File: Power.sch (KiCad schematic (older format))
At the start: 27 parts, among them J3 Conn_01x02, Q1 MMBT5401LT1G, Q2 Q_NMOS_GDS, Q3 MMBT3904, Q4 Q_NMOS_GDS, U6 LM5066

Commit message: Added protection from motor regeneration through capacitors + MOSFET, started placement and routing
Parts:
- added C32, C33, C34, C35, C36, C37: 330u, Capacitor_SMD:CP_Elec_18x17.5, symbol Device:CP_Small
- added C38, C39: 1u, Capacitor_SMD:C_0603_1608Metric, symbol Device:C_Small
- added C40: 100n, Capacitor_SMD:C_0603_1608Metric, symbol Device:C_Small
- added J4: Conn_01x02, Connector_PinHeader_2.54mm:PinHeader_1x02_P2.54mm_Horizontal, symbol Connector_Generic:Conn_01x02
- added Q5: Q_NMOS_GDS, Package_TO_SOT_SMD:TO-263-2, symbol Device:Q_NMOS_GDS
- added R21: 10R, Package_TO_SOT_THT:TO-247-2_Vertical, symbol Device:R_Small
- added R22: 100k, Resistor_SMD:R_0603_1608Metric, symbol Device:R_Small
- added R23: 49.9k, Resistor_SMD:R_0603_1608Metric, symbol Device:R_Small
- added R24: 2.7k, Resistor_SMD:R_0603_1608Metric, symbol Device:R_Small
- added R25: 82.5k, Resistor_SMD:R_0805_2012Metric, symbol Device:R_Small
- added R26, R28: 24.9k, Resistor_SMD:R_0805_2012Metric, symbol Device:R_Small
- added R27: 75k, Resistor_SMD:R_0805_2012Metric, symbol Device:R_Small
- added R29: 2M, Resistor_SMD:R_0603_1608Metric, symbol Device:R_Small
- added U7: LM311, Package_SO:SOIC-8_3.9x4.9mm_P1.27mm, symbol Comparator:LM311
- added U8: LR8K4-G, Package_TO_SOT_SMD:TO-252-2, symbol Regulator_Linear:LR8K4-G
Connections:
- net labels added: +24V, PROT_DRAIN
- wire segments 102 -> 155
- no-connect marks 5 -> 7
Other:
- note added: "Assuming VIN = 48V, Schmitt trigger\nTurn on at 52.1\nTurn off at 51.1"
- note added: "TODO power resistor and capacitance"
- note added: "TODO: Check if pin header compatible with Anderson connector"
- note added: "TODO: Check input cap for LDO"
- moved on the sheet: D5, D6, Q4, R18, R19, R20

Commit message: WIP with component placement
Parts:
- removed C33, C34, C35, C36, C37: 330u, Capacitor_SMD:CP_Elec_18x17.5, symbol Device:CP_Small
- removed C40: 100n, Capacitor_SMD:C_0603_1608Metric, symbol Device:C_Small
- removed R29: 2M, Resistor_SMD:R_0603_1608Metric, symbol Device:R_Small
- removed U7: LM311, Package_SO:SOIC-8_3.9x4.9mm_P1.27mm, symbol Comparator:LM311
- added C33, C34, C35: 100n, Capacitor_SMD:C_0603_1608Metric, symbol Device:C_Small
- added C36: 1nF, Capacitor_SMD:C_0603_1608Metric, symbol Device:C_Small
- added J5: Conn_ARM_JTAG_SWD_10, Connector_PinHeader_1.27mm:PinHeader_2x05_P1.27mm_Vertical, symbol Connector:Conn_ARM_JTAG_SWD_10
- added U7: STM32L011K4Tx, Package_QFP:LQFP-32_7x7mm_P0.8mm, symbol MCU_ST_STM32L0:STM32L011K4Tx
- C32: value 330u -> 470u
- C38: footprint Capacitor_SMD:C_0603_1608Metric -> Capacitor_SMD:C_1206_3216Metric
- C39: footprint Capacitor_SMD:C_0603_1608Metric -> Capacitor_SMD:C_0805_2012Metric
- J4: footprint Connector_PinHeader_2.54mm:PinHeader_1x02_P2.54mm_Horizontal -> Connectors_OSRF:PP45_1X2
- R23: value 49.9k -> 18.2K
- R24: value 2.7k -> 11.5K
- R25: value 82.5k -> 82.9k
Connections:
- net labels added: +3.3VP, SWDCLK, SWDIO, nRST
- net labels removed: +24V, PROT_DRAIN
- wire segments 155 -> 162
- no-connect marks 7 -> 5
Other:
- note removed: "Assuming VIN = 48V, Schmitt trigger\nTurn on at 52.1\nTurn off at 51.1"
- moved on the sheet: C29, C32, J3, J4, Q3, Q5, R21, R22, R25, R26, R27, R28

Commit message: Finished schematic, placement and routing, only silkscreen TODO
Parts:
- removed R23: 18.2K, Resistor_SMD:R_0603_1608Metric, symbol Device:R_Small
- removed R24: 11.5K, Resistor_SMD:R_0603_1608Metric, symbol Device:R_Small
- removed U8: LR8K4-G, Package_TO_SOT_SMD:TO-252-2, symbol Regulator_Linear:LR8K4-G
- added C37: 1u, Capacitor_SMD:C_1206_3216Metric, symbol Device:C_Small
- added U9: MAXM15062, DCDC:MAXIM_uSLIP-10, symbol DCDC_Converters:MAXM15062
- C31: footprint Capacitor_SMD:C_0603_1608Metric -> Capacitor_SMD:C_0402_1005Metric
- C38: footprint Capacitor_SMD:C_1206_3216Metric -> Capacitor_SMD:C_0603_1608Metric
- C39: value 1u -> 10u; footprint Capacitor_SMD:C_0805_2012Metric -> Capacitor_SMD:C_1206_3216Metric
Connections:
- net labels removed: LM_VDD
- wire segments 162 -> 168
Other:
- note removed: "TODO power resistor and capacitance"
- note removed: "TODO: Check if pin header compatible with Anderson connector"
- note removed: "TODO: Check input cap for LDO"
- moved on the sheet: C32, C33, C34, C35, J5, Q5, R21, R22, R25, R26, R27, R28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

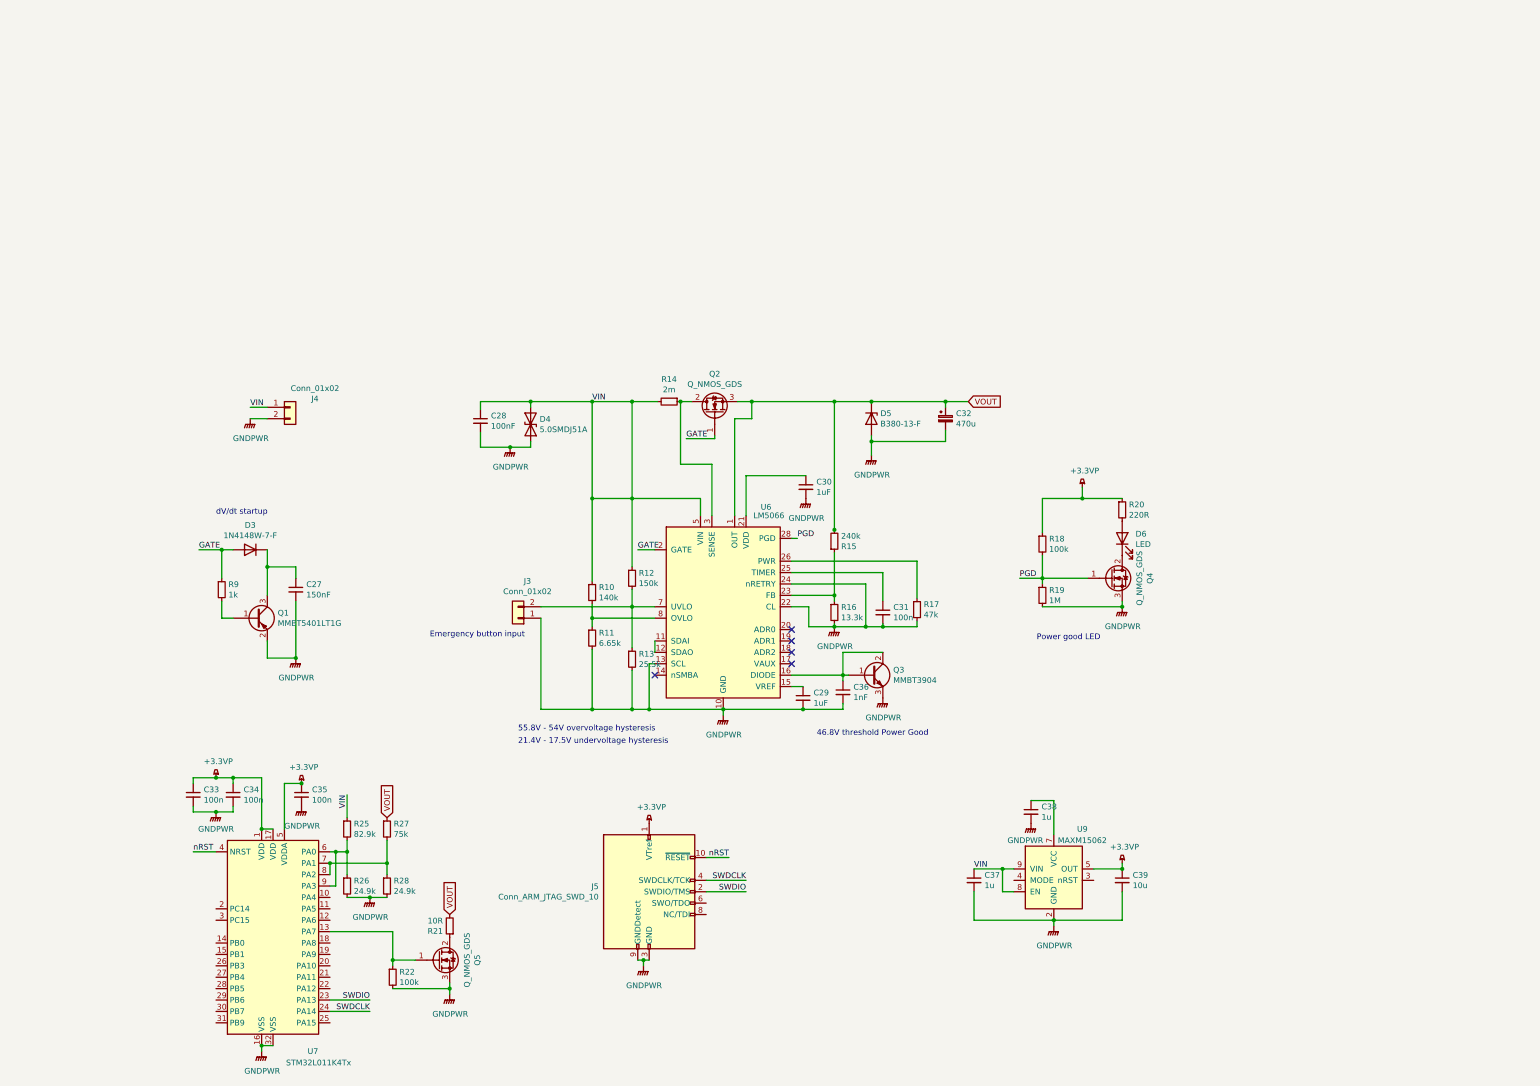
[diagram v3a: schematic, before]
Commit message: Fixed flipped connector, changed most placement
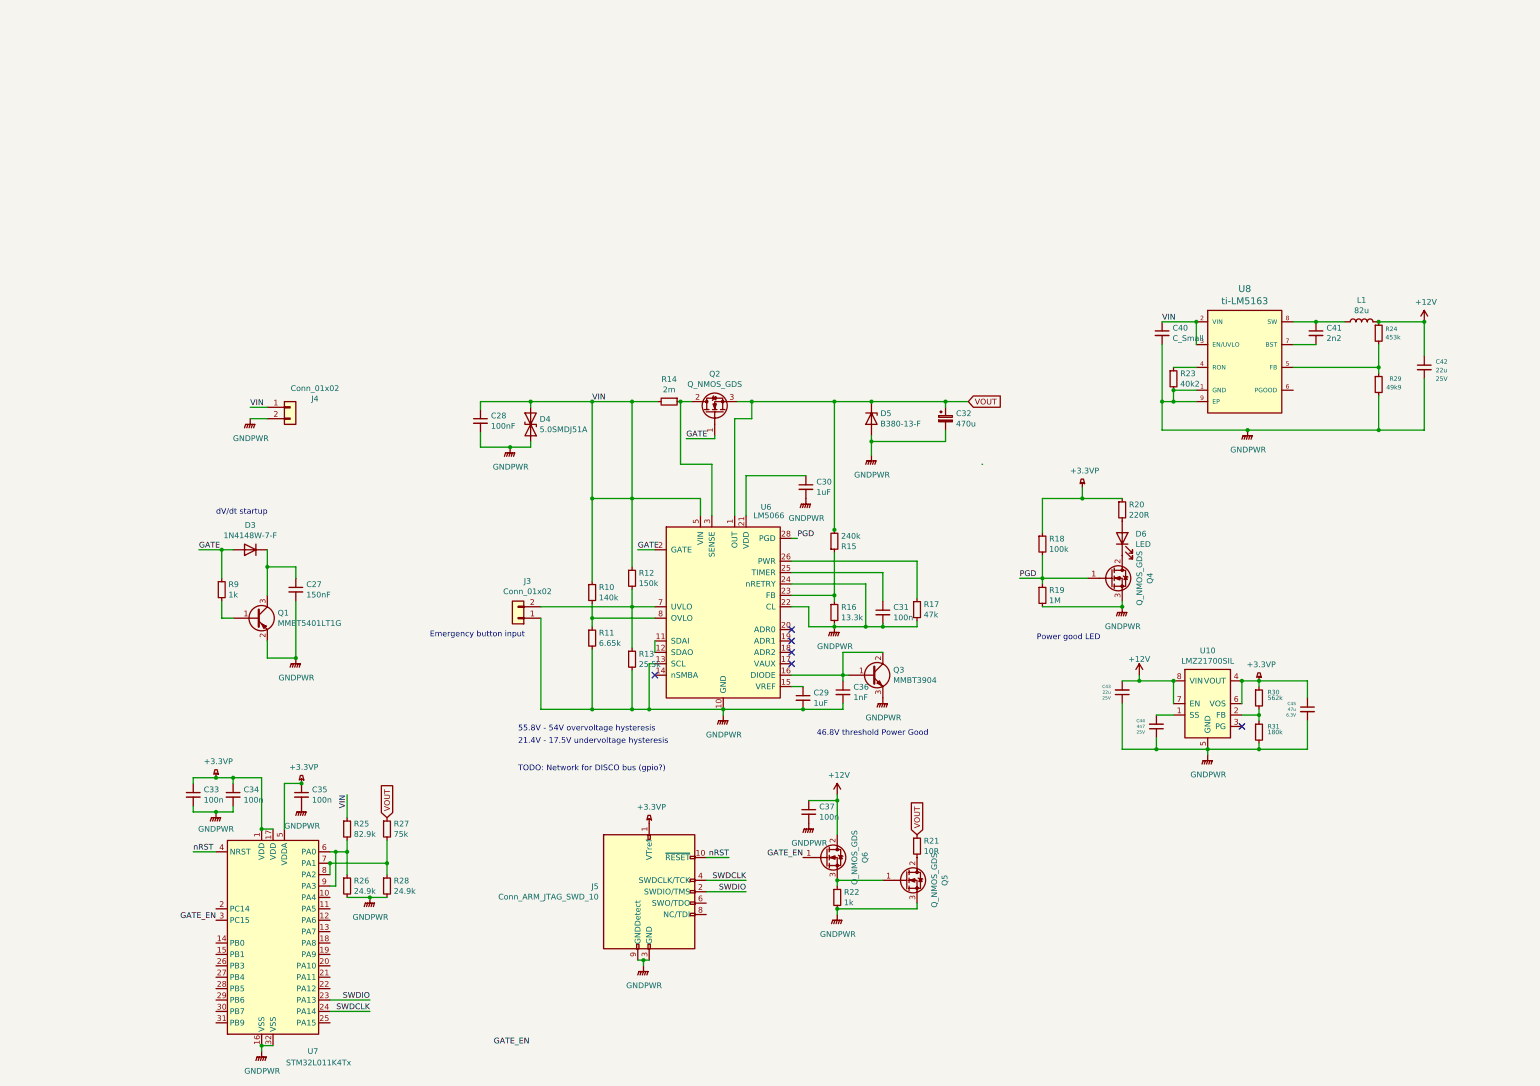
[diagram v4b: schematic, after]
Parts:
- removed C38: 1u, Capacitor_SMD:C_0603_1608Metric, symbol Device:C_Small
- removed C39: 10u, Capacitor_SMD:C_1206_3216Metric, symbol Device:C_Small
- removed U9: MAXM15062, DCDC:MAXIM_uSLIP-10, symbol DCDC_Converters:MAXM15062
- added C40: C_Small, Capacitor_SMD:C_1210_3225Metric, symbol Device:C_Small
- added C41: 2n2, Capacitor_SMD:C_0603_1608Metric, symbol Device:C_Small
- added C42: 22u, Capacitor_SMD:C_1210_3225Metric, symbol Device:C_Small
- added C43: 22u, Capacitor_SMD:C_1206_3216Metric, symbol Device:C_Small
- added C44: 4n7, Capacitor_SMD:C_0402_1005Metric, symbol Device:C_Small
- added C45: 47u, Capacitor_SMD:C_1206_3216Metric, symbol Device:C_Small
- added L1: 82u, Inductor_SMD:L_7.3x7.3_H4.5, symbol Device:L
- added Q6: Q_NMOS_GDS, Package_TO_SOT_SMD:SOT-416, symbol Device:Q_NMOS_GDS
- added R23: 40k2, Resistor_SMD:R_0805_2012Metric, symbol Device:R_Small
- added R24: 453k, Resistor_SMD:R_0603_1608Metric, symbol Device:R_Small
- added R29: 49k9, Resistor_SMD:R_0603_1608Metric, symbol Device:R_Small
- added R30: 562k, Resistor_SMD:R_0402_1005Metric, symbol Device:R_Small
- added R31: 180k, Resistor_SMD:R_0402_1005Metric, symbol Device:R_Small
- added U10: LMZ21700SIL, BLDC:SIL0008E, symbol BLDC:LMZ21700SILT
- added U8: ti-LM5163, Package_SO:SOIC-8-1EP_3.9x4.9mm_P1.27mm_EP2.41x3.3mm, symbol BLDC:ti-LM5163
- C31: footprint Capacitor_SMD:C_0402_1005Metric -> Capacitor_SMD:C_0603_1608Metric
- C37: value 1u -> 100n; footprint Capacitor_SMD:C_1206_3216Metric -> Capacitor_SMD:C_0603_1608Metric
- R22: value 100k -> 1k
- R25, R26, R27, R28: footprint Resistor_SMD:R_0805_2012Metric -> Resistor_SMD:R_0603_1608Metric
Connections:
- net +3.3VP: now also C45.1, R30.1, U10.4 (VOUT), U10.6 (VOS)
- net GNDPWR: now also C40.2, C42.2, C43.1, C44.1, C45.2, R23.2, R29.2, R31.2, U10.5 (GND), U10.9 (PAD), U8.1 (GND), U8.9 (EP)
- net VIN: now also C40.1, U8.2 (VIN), U8.3 (EN/UVLO); no longer C37.1
- net VOUT: now also R21.1; no longer R21.2
- net at Q5.1 (G), R22.1: now also Q6.3 (S); no longer U7.13 (PA7)
- net at Q5.2 (D): now also R21.2; no longer R21.1
- net GATE_EN: now reaches U7.3 (PC15)
- net GATE_EN: now also Q6.1 (G)
- new net: R23.1, U8.4 (RON)
- new net: R24.2, R29.1, U8.5 (FB)
- new net: C41.2, U8.7 (BST)
- new net: C41.1, L1.1, U8.8 (SW)
- new net: C44.2, U10.1 (SS)
- new net: R30.2, R31.1, U10.2 (FB)
- new net +12V: C37.1, C42.1, C43.2, L1.2, Q6.2 (D), R24.1, U10.7 (EN), U10.8 (VIN)
- no-connect marks 5 -> 6
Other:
- note added: "TODO: Network for DISCO bus (gpio?)"
- moved on the sheet: Q5, R21, R22

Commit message: Silk screen and cosmetic fixes
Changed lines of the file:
@@
 Wire Wire Line
 	10695 4600 10700 4600
-Wire Wire Line
-	8270 2100 8275 2100
 Connection ~ 9950 4000
 Connection ~ 10250 4600

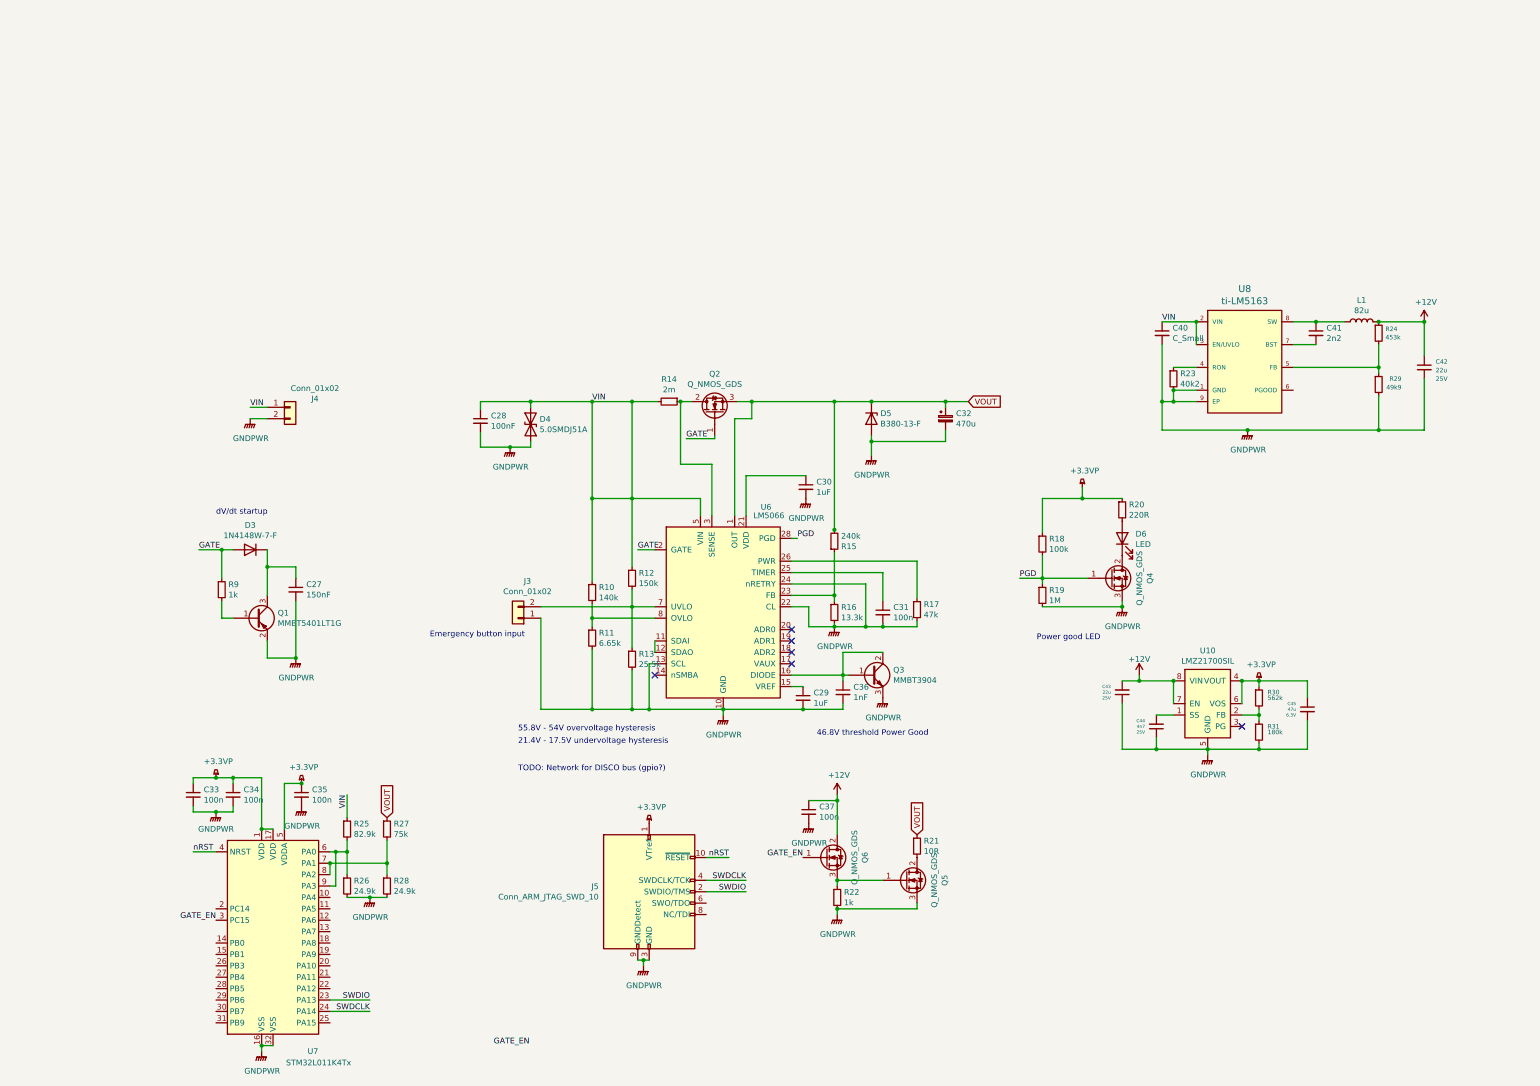
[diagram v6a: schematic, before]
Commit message: Changed voltage regulator, added I2C interface
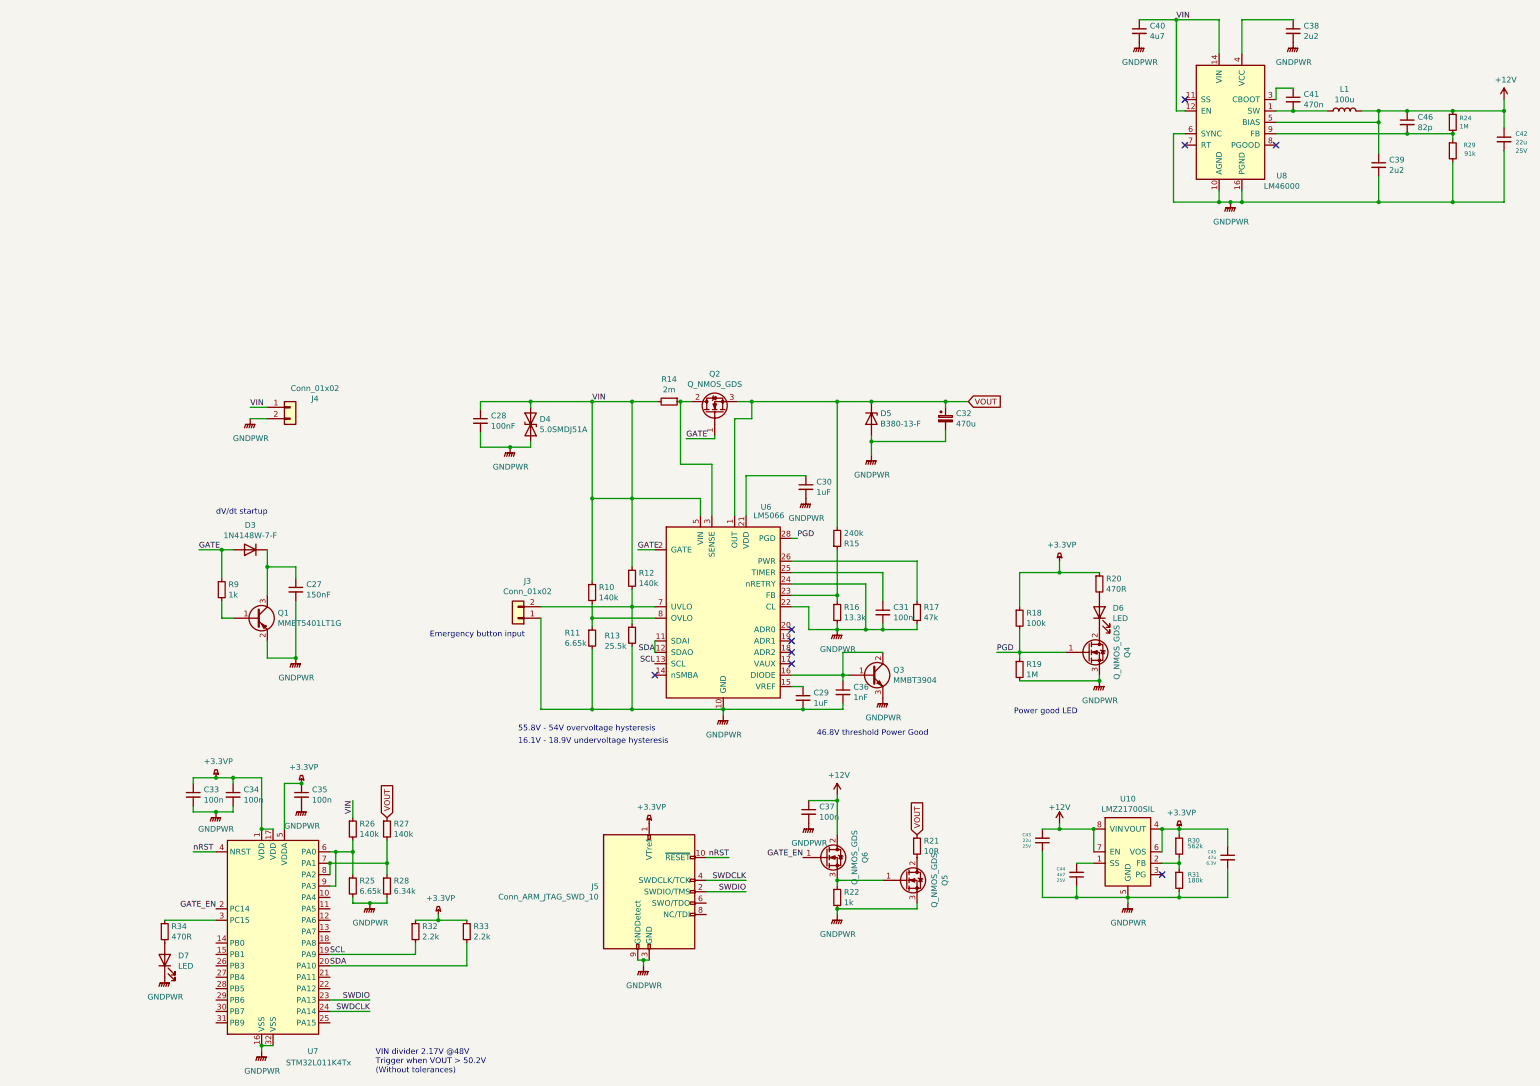
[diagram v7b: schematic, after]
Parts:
- removed R23: 40k2, Resistor_SMD:R_0805_2012Metric, symbol Device:R_Small
- removed U8: ti-LM5163, Package_SO:SOIC-8-1EP_3.9x4.9mm_P1.27mm_EP2.41x3.3mm, symbol BLDC:ti-LM5163
- added C38, C39: 2u2, Capacitor_SMD:C_0603_1608Metric, symbol Device:C_Small
- added C46: 82p, Capacitor_SMD:C_0603_1608Metric, symbol Device:C_Small
- added D7: LED, LED_SMD:LED_0603_1608Metric, symbol Device:LED
- added R32, R33: 2.2k, Resistor_SMD:R_0603_1608Metric, symbol Device:R_Small
- added R34: 470R, Resistor_SMD:R_0603_1608Metric, symbol Device:R_Small
- added U8: LM46000, BLDC:PWP0016G, symbol BLDC:LM46000
- C40: value C_Small -> 4u7
- C41: value 2n2 -> 470n
- L1: value 82u -> 100u
- R12: value 150k -> 140k
- R20: value 220R -> 470R
- R24: value 453k -> 1M
- R25: value 82.9k -> 6.65k
- R26: value 24.9k -> 140k
- R27: value 75k -> 140k
- R28: value 24.9k -> 6.34k
- R29: value 49k9 -> 91k
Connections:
- net +12V: now also C39.1, C46.1, U8.5 (BIAS)
- net +3.3VP: now also R32.1, R33.1
- net GATE_EN: now also U7.2 (PC14); no longer U7.3 (PC15)
- net GNDPWR: now also R25.2, C38.2, C39.2, D7.1 (K), U8.10 (AGND), U8.15 (PGND), U8.16 (PGND), U8.17 (AGND), U8.6 (SYNC); no longer R26.2, U6.13 (SCL)
- net VIN: now also R26.1, U8.12 (EN), U8.13 (VIN), U8.14 (VIN); no longer R25.1
- net at U7.6 (PA0), U7.9 (PA3): now also R25.1, R26.2; no longer R25.2, R26.1
- net SDA: now reaches U6.11 (SDAI), U6.12 (SDAO)
- net SDA: now also U7.20 (PA10), R33.2
- net SCL: now reaches U7.19 (PA9)
- net SCL: now also U6.13 (SCL), R32.2
- net at R24.2, R29.1: now also C46.2, U8.9 (FB)
- net at C41.2: now also L1.1, U8.1 (SW), U8.2 (SW)
- net at C41.1: now also U8.3 (CBOOT); no longer L1.1
- new net: R34.1, U7.3 (PC15)
- new net: C38.1, U8.4 (VCC)
- new net: D7.2 (A), R34.2
- no-connect marks 6 -> 9
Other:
- note added: "16.1V - 18.9V undervoltage hysteresis"
- note added: "VIN divider 2.17V @48V\nTrigger when VOUT > 50.2V\n(Without tolerances)"
- note removed: "21.4V - 17.5V undervoltage hysteresis"
- note removed: "TODO: Network for DISCO bus (gpio?)"
- moved on the sheet: C40, C41, C42, C43, C44, C45, D6, L1, Q4, R13, R15, R16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
